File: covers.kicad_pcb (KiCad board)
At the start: 2 copper layers, 28.9 x 74.3 mm, 5 parts

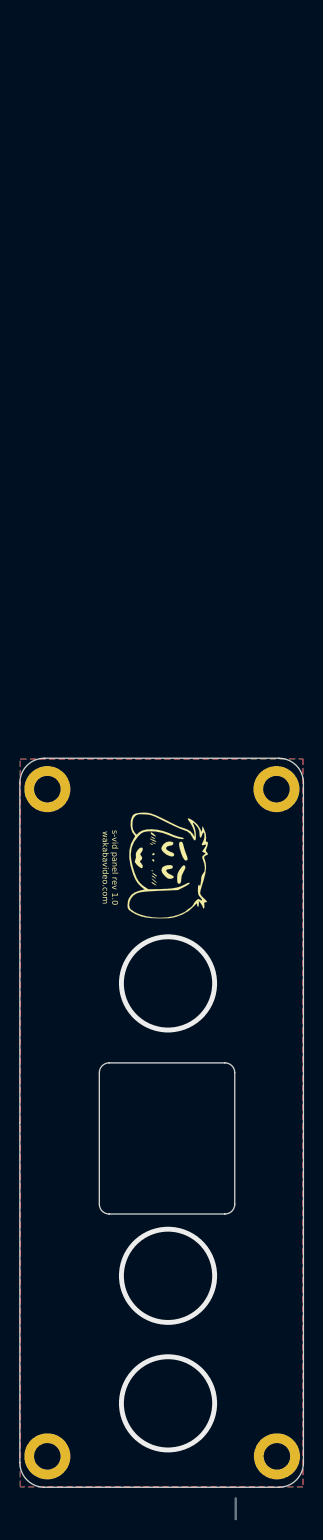
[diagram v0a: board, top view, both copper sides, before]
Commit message: updated gerbs, kicad 6 migration
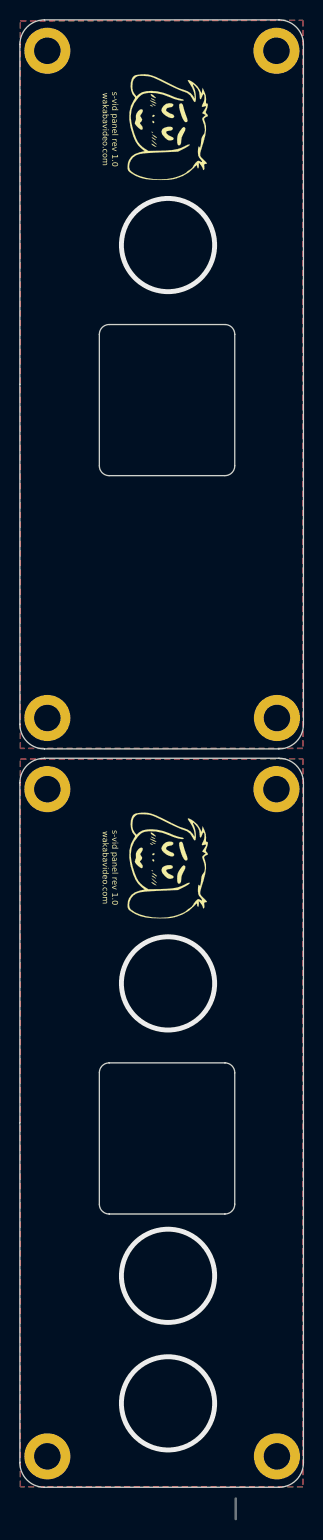
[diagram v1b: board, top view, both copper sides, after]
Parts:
- added G***: LOGO, videobits:uwuriel, F.Cu at (121.1, 49.9)
- added H12: MountingHole_Pad, MountingHole:MountingHole_2.7mm_M2.5_DIN965_Pad, F.Cu at (108.8, 110.0)
- added H16: MountingHole_Pad, MountingHole:MountingHole_2.7mm_M2.5_DIN965_Pad, F.Cu at (132.2, 110.0)
- added H4: MountingHole_Pad, MountingHole:MountingHole_2.7mm_M2.5_DIN965_Pad, F.Cu at (108.8, 42.0)
- added H8: MountingHole_Pad, MountingHole:MountingHole_2.7mm_M2.5_DIN965_Pad, F.Cu at (132.2, 42.0)
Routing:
- net /GND4: vias 3 -> 4
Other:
- board size 28.9 x 74.3 mm -> 28.9 x 149.5 mm
- net class Default removed
